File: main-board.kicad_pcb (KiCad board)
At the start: 4 copper layers, 140 x 97 mm, 30 parts, among them P1004 Rocker Switch, P10091 Molex PicoBlade 6 Right, P10092 Molex PicoBlade 6 Right, P10093 Molex PicoBlade 6 Right, P10094 Molex PicoBlade 6 Right, U10029 Small Buzzer

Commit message: Start placing parts on pcb.
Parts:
- removed ? (x4): , 
- removed B100: XT60PW, REV(5).IntLib:XT60PW
- removed Dribbler, MOTOR_2, MOTOR_3, MOTOR_4: S8B-XH-A, Miscellaneous Connectors.IntLib:S8B-XH-A-1
- removed IR: S4B-XH-A, Miscellaneous Connectors.IntLib:S4B-XH-A
- removed MOTOR_1: S8B-XH-A, ST Interface Stepper Motor Controller.IntLib:S8B-XH-A-1
- removed MikonaPOW: DS1072-2M-R, REV(5).IntLib:DS1072-2M&F-R
- removed P1004: Rocker Switch, REV(5).IntLib:Rocker_SW
- removed P10091, P10092, P10093, P10094: Molex PicoBlade 6 Right, SamatecLib.IntLib:Molex PicoBlade 6 Right SMD
- removed S_D_100: SW-PB, REV(5).IntLib:SPST-2
- removed S_ID100: ERD116RSZ, REV(5).IntLib:ERD116RSZ
- removed S_SET100: SW-DIP4, REV(5).IntLib:DIP-8-SW
- removed U10029: Small Buzzer, REV(5).IntLib:my_BUZZER
- added BZ501: Buzzer, Buzzer_Beeper:MagneticBuzzer_CUI_CMT-8504-100-SMT, F.Cu at (190.1, 140.5)
- added C201: 100nF, Capacitor_SMD:C_0603_1608Metric, F.Cu at (444.1, 21.7)
- added C301: 10nF, Capacitor_SMD:C_0805_2012Metric, F.Cu at (432.8, 80.1)
- added C302: 470nF, Capacitor_SMD:C_0603_1608Metric, F.Cu at (441.4, 79.9)
- added C303: 100nF, Capacitor_SMD:C_0603_1608Metric, F.Cu at (441.4, 82.4)
- added C304: 180nF, Capacitor_SMD:C_0603_1608Metric, F.Cu at (441.4, 84.9)
- added C305: 10uF, Capacitor_SMD:C_0805_2012Metric, F.Cu at (432.8, 83.1)
- added C306: 10uF, Capacitor_SMD:C_0805_2012Metric, F.Cu at (432.8, 86.1)
- added C307: 10uF, Capacitor_SMD:C_0805_2012Metric, F.Cu at (432.8, 89.1)
- added C308: 10uF, Capacitor_SMD:C_0805_2012Metric, F.Cu at (432.8, 92.2)
- added C309: 100nF, Capacitor_SMD:C_0603_1608Metric, F.Cu at (441.4, 87.4)
- added C310: 100uF, Capacitor_Tantalum_SMD:CP_EIA-7343-31_Kemet-D, F.Cu at (456.4, 92.9)
- added C311: 10uF 35v, Capacitor_SMD:C_0805_2012Metric, F.Cu at (432.8, 95.2)
- added C312: 10uF 35v, Capacitor_SMD:C_0805_2012Metric, F.Cu at (437.2, 80.1)
- added C313: 10uF 35v, Capacitor_SMD:C_0805_2012Metric, F.Cu at (437.2, 83.1)
- added C314: 10uF 35v, Capacitor_SMD:C_0805_2012Metric, F.Cu at (437.2, 86.1)
- added C315: 10uF 35v, Capacitor_SMD:C_0805_2012Metric, F.Cu at (437.2, 89.1)
- added C316: 10uF 35v, Capacitor_SMD:C_0805_2012Metric, F.Cu at (437.2, 92.2)
- added C317: 100nF, Capacitor_SMD:C_0603_1608Metric, F.Cu at (441.4, 89.9)
- added C318: 1.2nF, Capacitor_SMD:C_0603_1608Metric, F.Cu at (441.4, 92.4)
- added C401: 4.7nF, Capacitor_SMD:C_0603_1608Metric, F.Cu at (437.0, 141.4)
- added C402: 4.7nF, Capacitor_SMD:C_0603_1608Metric, F.Cu at (437.0, 143.9)
- added C403: 4.7nF, Capacitor_SMD:C_0603_1608Metric, F.Cu at (437.0, 146.4)
- added C404: 100nF, Capacitor_SMD:C_0603_1608Metric, F.Cu at (437.0, 148.9)
- added C405: 100nF, Capacitor_SMD:C_0603_1608Metric, F.Cu at (437.0, 151.4)
- added C406: 100nF, Capacitor_SMD:C_0603_1608Metric, F.Cu at (437.0, 154.0)
- added C407: 6pF, Capacitor_SMD:C_0603_1608Metric, F.Cu at (441.0, 141.4)
- added C408: 6pF, Capacitor_SMD:C_0603_1608Metric, F.Cu at (441.0, 143.9)
- added C501: 100nF, Capacitor_SMD:C_0603_1608Metric, F.Cu at (403.0, 117.4)
- added C502: 100nF, Capacitor_SMD:C_0603_1608Metric, F.Cu at (403.0, 119.9)
- added C503: 100nF, Capacitor_SMD:C_0603_1608Metric, F.Cu at (403.0, 122.4)
- added C504: 100nF, Capacitor_SMD:C_0603_1608Metric, F.Cu at (403.0, 124.9)
- added C505: 100nF, Capacitor_SMD:C_0603_1608Metric, F.Cu at (403.0, 127.4)
- added C506: 100nF, Capacitor_SMD:C_0603_1608Metric, F.Cu at (403.0, 129.9)
- added C507: 100nF, Capacitor_SMD:C_0603_1608Metric, F.Cu at (403.0, 132.4)
- added C508: 100nF, Capacitor_SMD:C_0603_1608Metric, F.Cu at (407.0, 117.4)
- added C509: 100nF, Capacitor_SMD:C_0603_1608Metric, F.Cu at (407.0, 119.9)
- added C510: 1uF, Capacitor_SMD:C_0603_1608Metric, F.Cu at (407.0, 122.4)
- added C511: 1uF, Capacitor_SMD:C_0603_1608Metric, F.Cu at (407.0, 124.9)
- added C512: 27pF, Capacitor_SMD:C_0603_1608Metric, F.Cu at (407.0, 127.4)
- added C513: 27pF, Capacitor_SMD:C_0603_1608Metric, F.Cu at (407.0, 129.9)
- added C514: 100nF, Capacitor_SMD:C_0603_1608Metric, F.Cu at (407.0, 132.4)
- added C601: 100nF, Capacitor_SMD:C_0603_1608Metric, F.Cu at (437.0, 117.4)
- added C602: 100nF, Capacitor_SMD:C_0603_1608Metric, F.Cu at (437.0, 119.9)
- added C603: 2.2uF, Capacitor_SMD:C_0805_2012Metric, F.Cu at (455.0, 135.2)
- added C604: 10nF, Capacitor_SMD:C_0603_1608Metric, F.Cu at (437.0, 122.4)
- added D201: LED Red, LED_SMD:LED_0603_1608Metric, F.Cu at (166.5, 91.2)
- added D202: LED Green, LED_SMD:LED_0603_1608Metric, F.Cu at (168.3, 91.2)
- added D501: LED Green, LED_SMD:LED_0603_1608Metric, F.Cu at (431.0, 147.8)
- added H101: MountingHole_Pad, MountingHole:MountingHole_3.2mm_M3_ISO14580_Pad, F.Cu at (87.5, 91.8)
- added H102: MountingHole_Pad, MountingHole:MountingHole_3.2mm_M3_ISO14580_Pad, F.Cu at (209.5, 91.8)
- added H103: MountingHole_Pad, MountingHole:MountingHole_3.2mm_M3_ISO14580_Pad, F.Cu at (109.7, 150.5)
- added H104: MountingHole_Pad, MountingHole:MountingHole_3.2mm_M3_ISO14580_Pad, F.Cu at (187.4, 150.5)
- added J101: Battery, Connector_AMASS:AMASS_XT60PW-M_1x02_P7.20mm_Horizontal, B.Cu at (122.5, 136.6)
- added J102: Mikona, 1054291104:MOLEX_1054291104, F.Cu at (413.9, 106.6)
- added J201: DSI, FH12-22S:Hirose_FH12-22S-0.5SH_1x22-1MP_P0.50mm_Horizontal, F.Cu at (175.5, 148.5)
- added J601: Qwiic, Connector_JST:JST_SH_SM04B-SRSS-TB_1x04-1MP_P1.00mm_Horizontal, F.Cu at (145.3, 59.5)
- added J602: S4B-XH-A, Connector_JST:JST_XH_S4B-XH-A_1x04_P2.50mm_Horizontal, B.Cu at (153.5, 65.9)
- added J705: ENC1, Connector_Molex:Molex_PicoBlade_53261-0671_1x06-1MP_P1.25mm_Horizontal, F.Cu at (82.6, 83.4)
- added J706: ENC2, Connector_Molex:Molex_PicoBlade_53261-0671_1x06-1MP_P1.25mm_Horizontal, F.Cu at (214.1, 83.4)
- added J707: M1, Connector_JST:JST_XH_S8B-XH-A_1x08_P2.50mm_Horizontal, B.Cu at (90.0, 77.2)
- added J708: M2, Connector_JST:JST_XH_S8B-XH-A_1x08_P2.50mm_Horizontal, B.Cu at (207.0, 59.7)
- added J711: ENC3, Connector_Molex:Molex_PicoBlade_53261-0671_1x06-1MP_P1.25mm_Horizontal, F.Cu at (214.1, 98.9)
- added J712: ENC4, Connector_Molex:Molex_PicoBlade_53261-0671_1x06-1MP_P1.25mm_Horizontal, F.Cu at (82.6, 98.9)
- added J713: M3, Connector_JST:JST_XH_S8B-XH-A_1x08_P2.50mm_Horizontal, B.Cu at (207.0, 105.3)
- added J714: M4, Connector_JST:JST_XH_S8B-XH-A_1x08_P2.50mm_Horizontal, B.Cu at (90.0, 122.8)
- added J717: ENCD, Connector_Molex:Molex_PicoBlade_53261-0671_1x06-1MP_P1.25mm_Horizontal, F.Cu at (126.9, 47.1)
- added J718: MD, Connector_JST:JST_XH_S8B-XH-A_1x08_P2.50mm_Horizontal, B.Cu at (120.0, 65.9)
- added L301: 3.3µH, Inductor_SMD:L_Bourns_SRN6045TA, F.Cu at (434.6, 100.4)
- added Module201: ComputeModule4-CM4, rpi-cm4:rpi-cm4, F.Cu at (125.7, 97.9)
- added Q301: BSC014N04LS, BSC014N04LSIATMA1:TRANS_BSC014N04LSIATMA1, F.Cu at (108.5, 141.5)
- added Q501: BSS138, Package_TO_SOT_SMD:SOT-23, F.Cu at (426.5, 148.7)
- added Q601: BSS138, Package_TO_SOT_SMD:SOT-23, F.Cu at (450.3, 135.9)
- added R101: 2mΩ, Resistor_SMD:R_2512_6332Metric, F.Cu at (424.2, 101.5)
- added R201: 0, Resistor_SMD:R_0603_1608Metric, F.Cu at (444.1, 24.3)
- added R202: 2.2K, Resistor_SMD:R_0603_1608Metric, F.Cu at (444.1, 26.8)
- added R203: 2.2K, Resistor_SMD:R_0603_1608Metric, F.Cu at (444.1, 29.3)
- added R204: 200, Resistor_SMD:R_0603_1608Metric, F.Cu at (444.1, 31.8)
- added R205: 1K, Resistor_SMD:R_0603_1608Metric, F.Cu at (444.1, 34.3)
- added R206: 1K, Resistor_SMD:R_0603_1608Metric, F.Cu at (444.1, 36.8)
- added R207: 200, Resistor_SMD:R_0603_1608Metric, F.Cu at (444.1, 39.3)
- added R301: 1mΩ, Resistor_SMD:R_2512_6332Metric, F.Cu at (443.8, 98.6)
- added R302: 2mΩ, Resistor_SMD:R_2512_6332Metric, F.Cu at (443.8, 103.5)
- added R303: 1K, Resistor_SMD:R_0603_1608Metric, F.Cu at (441.4, 94.9)
- added R304: 1M, Resistor_SMD:R_0603_1608Metric, F.Cu at (445.5, 79.9)
- added R305: 1K, Resistor_SMD:R_0603_1608Metric, F.Cu at (445.5, 82.4)
- added R306: 5.6K, Resistor_SMD:R_0603_1608Metric, F.Cu at (445.5, 84.9)
- added R307: 40.2K, Resistor_SMD:R_0603_1608Metric, F.Cu at (445.5, 87.4)
- added R308: 1K, Resistor_SMD:R_0603_1608Metric, F.Cu at (445.5, 89.9)
- added R309: 24K, Resistor_SMD:R_0603_1608Metric, F.Cu at (445.5, 92.4)
- added R310: 10, Resistor_SMD:R_0603_1608Metric, F.Cu at (445.5, 94.9)
- added R311: 1K, Resistor_SMD:R_0603_1608Metric, F.Cu at (449.5, 79.9)
- added R312: 12K 1%, Resistor_SMD:R_0603_1608Metric, F.Cu at (449.5, 82.4)
- added R313: 20K 1%, Resistor_SMD:R_0603_1608Metric, F.Cu at (449.5, 84.9)
- added R314: 2.2K 1%, Resistor_SMD:R_0603_1608Metric, F.Cu at (449.5, 87.4)
- added R401: 60.4, Resistor_SMD:R_0603_1608Metric, F.Cu at (441.0, 146.4)
- added R402: 0, Resistor_SMD:R_0603_1608Metric, F.Cu at (441.0, 148.9)
- added R403: 60.4, Resistor_SMD:R_0603_1608Metric, F.Cu at (441.0, 151.4)
- added R501: 0, Resistor_SMD:R_0603_1608Metric, F.Cu at (411.0, 117.4)
- added R502: 1K, Resistor_SMD:R_0603_1608Metric, F.Cu at (411.0, 119.9)
- added R503: 1K, Resistor_SMD:R_0603_1608Metric, F.Cu at (411.0, 122.4)
- added R504: 10K, Resistor_SMD:R_0603_1608Metric, F.Cu at (411.0, 124.9)
- added R601: 300, Resistor_SMD:R_0603_1608Metric, F.Cu at (437.0, 124.9)
- added R602: 36, Resistor_SMD:R_0603_1608Metric, F.Cu at (437.0, 127.4)
- added R603: 0, Resistor_SMD:R_0603_1608Metric, F.Cu at (437.0, 129.9)
- added RN501: 1.8K, Resistor_SMD:R_Array_Concave_4x0603, F.Cu at (426.1, 144.1)
- added RN502: 10K, Resistor_SMD:R_Array_Concave_4x0603, F.Cu at (430.3, 144.1)
- added SW201: SW_Push, Button_Switch_SMD:SW_SPST_B3U-1000P, F.Cu at (162.3, 90.4)
- added SW202: SW_Push, Button_Switch_SMD:SW_SPST_B3U-1000P, F.Cu at (158.1, 90.4)
- added SW301: SW_Push, Button_Switch_THT:SW_Tactile_SPST_Angled_PTS645Vx58-2LFS, B.Cu at (92.3, 135.6)
- added SW501: SW_Coded_SH-7050, Button_Switch_SMD:Nidec_Copal_SH-7010A, F.Cu at (139.5, 140.5)
- added SW502: SW_DIP_x04, Button_Switch_SMD:SW_DIP_SPSTx04_Slide_6.7x11.72mm_W6.73mm_P2.54mm_LowProfile_JPin, F.Cu at (151.1, 140.6)
- added SW503: S_D_2, Button_Switch_SMD:SW_Push_1P1T_NO_6x6mm_H9.5mm, F.Cu at (163.2, 140.6)
- added U1: ~, Immortals:motor-driver, F.Cu at (93.4, 86.6)
- added U2: ~, Immortals:motor-driver, F.Cu at (180.5, 86.6)
- added U201: 74154, 74HC154:DHVQFN24, F.Cu at (455.7, 55.4)
- added U202: 74LVC1G07SE-7, Package_TO_SOT_SMD:SOT-353_SC-70-5, F.Cu at (441.9, 61.4)
- added U3: ~, Immortals:motor-driver, F.Cu at (203.3, 97.9)
- added U301: LTC2955CTS8-1, Package_TO_SOT_SMD:TSOT-23-8, F.Cu at (104.7, 135.6)
- added U302: PAC1954, Package_DFN_QFN:VQFN-16-1EP_3x3mm_P0.5mm_EP1.1x1.1mm, F.Cu at (459.2, 105.5)
- added U303: LTC4231-2, Package_SO:MSOP-12_3x4mm_P0.65mm, F.Cu at (111.9, 135.0)
- added U304: AP64501SP-13, Package_SO:SOIC-8-1EP_3.9x4.9mm_P1.27mm_EP2.95x4.9mm_Mask2.71x3.4mm_ThermalVias, F.Cu at (452.4, 106.1)
- added U4: ~, Immortals:motor-driver, F.Cu at (116.2, 97.9)
- added U401: MCP251863, Package_SO:SSOP-28_5.3x10.2mm_P0.65mm, F.Cu at (448.3, 146.2)
- added U5: ~, Immortals:motor-driver, F.Cu at (148.5, 92.0)
- added U501: RP2040, Package_DFN_QFN:QFN-56-1EP_7x7mm_P0.4mm_EP3.2x3.2mm, F.Cu at (417.7, 132.2)
- added U502: 74LS151, Package_SO:SOIC-16_3.9x9.9mm_P1.27mm, F.Cu at (417.2, 121.8)
- added U503: W25Q128JVS, Package_SO:SOIC-8_5.23x5.23mm_P1.27mm, F.Cu at (418.2, 147.8)
- added U601: ICM-42688-P, ICM-42688-P:PQFN50P300X250X97-14N, F.Cu at (450.6, 131.7)
- added Y401: 40MHz, Crystal:Crystal_SMD_2016-4Pin_2.0x1.6mm, F.Cu at (444.9, 154.0)
- added Y501: 12MHz, Crystal:Crystal_SMD_5032-2Pin_5.0x3.2mm, F.Cu at (427.7, 139.3)

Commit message: Place all the components on the PCB.
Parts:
- removed Booster: S6B-XH-A, Miscellaneous Connectors.IntLib:S6B-XH-A
- C301, C302, C303, C305, C306, C307, C308, C309, C310, C311, C312, C313, C314, C315, C316, C317, C318, C401, C402, C403, C404, C405, C406, C407, C408, C501, C502, C503, C504, C505, C506, C507, C508, C509, C510, C511, L301, R101, R202, R203, R303, R305, R308, R310, R311, R312, R313, R314, R401, R402, R403, RN501, RN502, U301, U302, U304, U401, U502, Y401: moved to B.Cu
- J102: footprint 1054291104:MOLEX_1054291104 -> 1054301204:MOLEX_1054301204; moved to B.Cu
- J602: value S4B-XH-A -> IR; footprint Connector_JST:JST_XH_S4B-XH-A_1x04_P2.50mm_Horizontal -> Connector_JST:JST_SH_SM04B-SRSS-TB_1x04-1MP_P1.00mm_Horizontal
- U1, U2, U3, U4, U5: footprint Immortals:motor-driver -> Immortals:MotorDriver-SMT
- moved R303 342.5 mm to (100.9, 131.8)
- moved R307 339.8 mm to (109.5, 138.8), turned to -90 degrees
- moved R309 339.6 mm to (109.5, 142.0), turned to -90 degrees
- moved R306 337.2 mm to (111.9, 134.2), turned to -90 degrees
- moved C302 336.9 mm to (108.7, 132.6), turned to -90 degrees
- moved C301 336.3 mm to (100.7, 133.6), turned to 180 degrees
- moved R304 336.0 mm to (113.9, 134.2), turned to 90 degrees
- moved C304 334.4 mm to (112.7, 146.2), turned to -90 degrees
- moved R314 333.8 mm to (116.8, 114.5), turned to -90 degrees
- moved R312 332.5 mm to (118.2, 110.9), turned to -90 degrees
- moved U304 332.0 mm to (120.5, 116.2), turned to 90 degrees
- moved R313 330.7 mm to (119.8, 110.9), turned to 90 degrees
- moved R302 328.8 mm to (117.7, 146.0)
- moved C310 327.7 mm to (128.9, 105.4), turned to 180 degrees
- moved U302 327.6 mm to (132.3, 127.8), turned to -90 degrees
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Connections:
- J101 pad 1: +BATT -> GND
- J101 pad 2: GND -> +BATT
- J102 pad 2: GND -> /CAN_N
- J102 pad 3: /CAN_N -> /CAN_P
- J102 pad 4: /CAN_P -> GND

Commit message: Finish the draft routing.
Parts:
- removed C401, C402, C403: 4.7nF, Capacitor_SMD:C_0603_1608Metric
- removed C404, C405, C406: 100nF, Capacitor_SMD:C_0603_1608Metric
- removed C407, C408: 6pF, Capacitor_SMD:C_0603_1608Metric
- removed D1, D_D_1: LED Red 1206, Miscellaneous Devices.IntLib:3.2X1.6X1.1 - RED
- removed D2, D_D_3: LED Green 1206, Miscellaneous Devices.IntLib:3.2X1.6X1.1 - GREEN
- removed D21: LED White 1206, Miscellaneous Devices.IntLib:3.2X1.6X1.1 - WHITE
- removed D24, D_D_2: LED Yellow 1206, Miscellaneous Devices.IntLib:3.2X1.6X1.1 - YELLOW
- removed D_D_4: LED Blue 1206, Miscellaneous Devices.IntLib:3.2X1.6X1.1 - BLUE
- removed R101: 2mΩ, Resistor_SMD:R_2512_6332Metric
- removed R401, R403: 60.4, Resistor_SMD:R_0603_1608Metric
- removed R402: 0, Resistor_SMD:R_0603_1608Metric
- removed RN501: 1.8K, Resistor_SMD:R_Array_Concave_4x0603
- removed U401: MCP251863, Package_SO:SSOP-28_5.3x10.2mm_P0.65mm
- removed Y401: 40MHz, Crystal:Crystal_SMD_2016-4Pin_2.0x1.6mm
- added D301: LED Green, LED_SMD:LED_0603_1608Metric, F.Cu at (138.0, 151.0)
- added R315: 1K, Resistor_SMD:R_0603_1608Metric, F.Cu at (138.0, 147.8)
- added R505: 1.8K, Resistor_SMD:R_0603_1608Metric, B.Cu at (152.6, 58.6)
- added R506: 1.8K, Resistor_SMD:R_0603_1608Metric, B.Cu at (151.0, 58.6)
- added R507: 1.8K, Resistor_SMD:R_0603_1608Metric, F.Cu at (159.6, 80.0)
- added R508: 1.8K, Resistor_SMD:R_0603_1608Metric, B.Cu at (159.6, 80.0)
- R311: value 1K -> 2mΩ
- U202: moved to B.Cu
- moved R204 31.1 mm to (131.2, 86.5)
- moved SW201 31.1 mm to (131.2, 90.7)
- moved R207 30.2 mm to (127.9, 86.5)
- moved SW202 30.2 mm to (127.9, 90.7)
- moved R205 28.9 mm to (136.2, 93.5)
- moved D201 28.9 mm to (136.2, 90.4)
- moved U202 27.1 mm to (137.5, 95.1)
- moved RN502 26.9 mm to (159.0, 115.0), turned to 90 degrees
- moved R311 21.2 mm to (121.2, 129.6), turned to -90 degrees
- moved R305 15.1 mm to (140.1, 117.6), turned to 180 degrees
- moved U502 13.0 mm to (153.2, 123.4)
- moved C303 10.8 mm to (141.8, 120.1), turned to -90 degrees
- moved U302 9.52 mm to (138.4, 120.5), turned to 180 degrees
- moved C512 6.71 mm to (162.8, 87.4)
- moved R502 6.60 mm to (168.4, 86.4)
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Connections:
- C305 pad 1: /Power/SENSE_5v+ -> +5V
- C306 pad 1: /Power/SENSE_5v+ -> +5V
- C307 pad 1: /Power/SENSE_5v+ -> +5V
- C308 pad 1: /Power/SENSE_5v+ -> +5V
- C310 pad 1: /Power/SENSE_5v+ -> +5V
- C311 pad 1: +BATT -> /Power/SENSE_5v-
- C312 pad 1: +BATT -> /Power/SENSE_5v-
- C313 pad 1: +BATT -> /Power/SENSE_5v-
- C314 pad 1: +BATT -> /Power/SENSE_5v-
- C315 pad 1: +BATT -> /Power/SENSE_5v-
- C316 pad 1: +BATT -> /Power/SENSE_5v-
- C503 pad 1: +3V3 -> +3.3V
- C504 pad 1: +3V3 -> +3.3V
- C505 pad 1: +3V3 -> +3.3V
- C506 pad 1: +3V3 -> +3.3V
- C507 pad 1: +3V3 -> +3.3V
- C508 pad 1: +3V3 -> +3.3V
- C509 pad 1: +3V3 -> +3.3V
- C511 pad 1: +3V3 -> +3.3V
- C514 pad 1: +3V3 -> +3.3V
- J102 pad 1: /SENSE_MIKONA -> +24V
- J102 pad 2: /CAN_N -> /MICRO_I2C0_SCL
- J102 pad 3: /CAN_P -> /MICRO_I2C0_SDA
- J102 pad SH: unconnected-(J102-Shield-PadSH) -> (no net)
- L301 pad 2: /Power/SENSE_5v+ -> +5V
- Module201 pad 29: /~{CM_SPI1_CS_MICRO} -> /Compute Module/SPI1_CE2
- Module201 pad 49: /~{CM_SPI1_CS_CAN} -> /~{CM_SPI1_CS_IMU}
- Module201 pad 50: /~{CM_SPI1_CS_IMU} -> /~{CM_SPI1_CS_MICRO}
- Module201 pad 56: /~{CAN_INT} -> /Compute Module/GPIO3
- R311 pad 1: +5V -> /Power/SENSE_5v-
- R311 pad 2: /Power/SENSE_5v+ -> +BATT
- R312 pad 1: /Power/SENSE_5v+ -> +5V
- R504 pad 1: +3V3 -> +3.3V
- RN502 pad 1: /Micro/DIP_0 -> /Micro/DIP_3
- RN502 pad 2: /Micro/DIP_1 -> /Micro/DIP_2
- RN502 pad 3: /Micro/DIP_2 -> /Micro/DIP_1
- RN502 pad 4: /Micro/DIP_3 -> /Micro/DIP_0
- U201 pad 1: /~{M1_SPI_CS_C} -> /~{MD_SPI_CS_C}
- U201 pad 10: /~{MD_SPI_CS_D} -> /~{M2_SPI_CS_D}
- U201 pad 2: /~{M1_SPI_CS_D} -> /~{MD_SPI_CS_D}
- U201 pad 3: /~{M2_SPI_CS_C} -> /~{M1_SPI_CS_C}
- U201 pad 4: /~{M2_SPI_CS_D} -> /~{M1_SPI_CS_D}
- U201 pad 5: /~{M3_SPI_CS_C} -> /~{M4_SPI_CS_C}
- U201 pad 6: /~{M3_SPI_CS_D} -> /~{M4_SPI_CS_D}
- U201 pad 7: /~{M4_SPI_CS_C} -> /~{M3_SPI_CS_C}
- U201 pad 8: /~{M4_SPI_CS_D} -> /~{M3_SPI_CS_D}
- U201 pad 9: /~{MD_SPI_CS_C} -> /~{M2_SPI_CS_C}
- U302 pad 13: /Power/SENSE_5v+ -> +24V
- U302 pad 14: +5V -> /Power/SENSE_5v-
- U302 pad 7: /SENSE_MIKONA -> unconnected-(U302-SENSE3--Pad7)
- U302 pad 8: +24V -> unconnected-(U302-SENSE3+-Pad8)
- U303 pad 9: /Power/PWR_STATUS -> Net-(D301-A)
- U304 pad 2: +BATT -> /Power/SENSE_5v-
- U501 pad 1: +3V3 -> +3.3V
- U501 pad 10: +3V3 -> +3.3V
- U501 pad 15: /Micro/MUX_S0 -> /Micro/MUX_O
- U501 pad 16: /Micro/MUX_S1 -> /Micro/MUX_S2
- U501 pad 17: /Micro/MUX_S2 -> /Micro/MUX_S1
- U501 pad 18: /Micro/MUX_O -> /Micro/MUX_S0
- U501 pad 22: +3V3 -> +3.3V
- U501 pad 26: +3V3 -> +3.3V
- U501 pad 33: +3V3 -> +3.3V
- U501 pad 42: +3V3 -> +3.3V
- U501 pad 43: +3V3 -> +3.3V
- U501 pad 44: +3V3 -> +3.3V
- U501 pad 48: +3V3 -> +3.3V
- U501 pad 49: +3V3 -> +3.3V
- U501 pad 8: /MD_C_S -> /MD_D_F
- U501 pad 9: /MD_D_F -> /MD_C_S
- U502 pad 1: /Micro/DIP_3 -> /Micro/ID_BIT_2
- U502 pad 12: /Micro/ID_BIT_3 -> /Micro/DIP_0
- U502 pad 13: /Micro/ID_BIT_2 -> /Micro/DIP_1
- U502 pad 14: /Micro/ID_BIT_1 -> /Micro/DIP_2
- U502 pad 15: /Micro/ID_BIT_0 -> /Micro/DIP_3
- U502 pad 2: /Micro/DIP_2 -> /Micro/ID_BIT_0
- U502 pad 3: /Micro/DIP_1 -> /Micro/ID_BIT_1
- U502 pad 4: /Micro/DIP_0 -> /Micro/ID_BIT_3
- U503 pad 8: +3V3 -> +3.3V
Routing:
- net GND: track 0.00 -> 328.2 mm, vias 0 -> 107
- net +3.3V: track 0.00 -> 273.2 mm, vias 0 -> 35
- net /M_SPI_MISO: track 0.00 -> 206.1 mm, vias 0 -> 2
- net /M_EN: track 0.00 -> 204.3 mm, vias 0 -> 11
- net /M_SPI_MOSI: track 0.00 -> 199.8 mm, vias 0 -> 2
- net /M_SPI_SCK: track 0.00 -> 160.3 mm
- net +5V: track 0.00 -> 136.4 mm, vias 0 -> 15
- net /MICRO_I2C0_SDA: track 0.00 -> 99.0 mm, vias 0 -> 1
- net /MICRO_I2C0_SCL: track 0.00 -> 89.2 mm, vias 0 -> 1
- net /M4_D_F: track 0.00 -> 86.3 mm, vias 0 -> 2
- net /Compute Module/ID_SC: track 0.00 -> 85.6 mm, vias 0 -> 5
- net /M1_C_S: track 0.00 -> 75.1 mm, vias 0 -> 2
- net /Micro/BUTTON: track 0.00 -> 73.1 mm, vias 0 -> 2
- net /~{POWER_OFF}: track 0.00 -> 72.8 mm, vias 0 -> 3
- net /~{M1_SPI_CS_C}: track 0.00 -> 68.8 mm, vias 0 -> 2
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- added copper zone on In1.Cu, net +24V
- added copper zone on In1.Cu, net +3.3V
- added copper zone on In1.Cu, net +5V
- added copper zone on In1.Cu, net GND
- added copper zone on In2.Cu, net GND

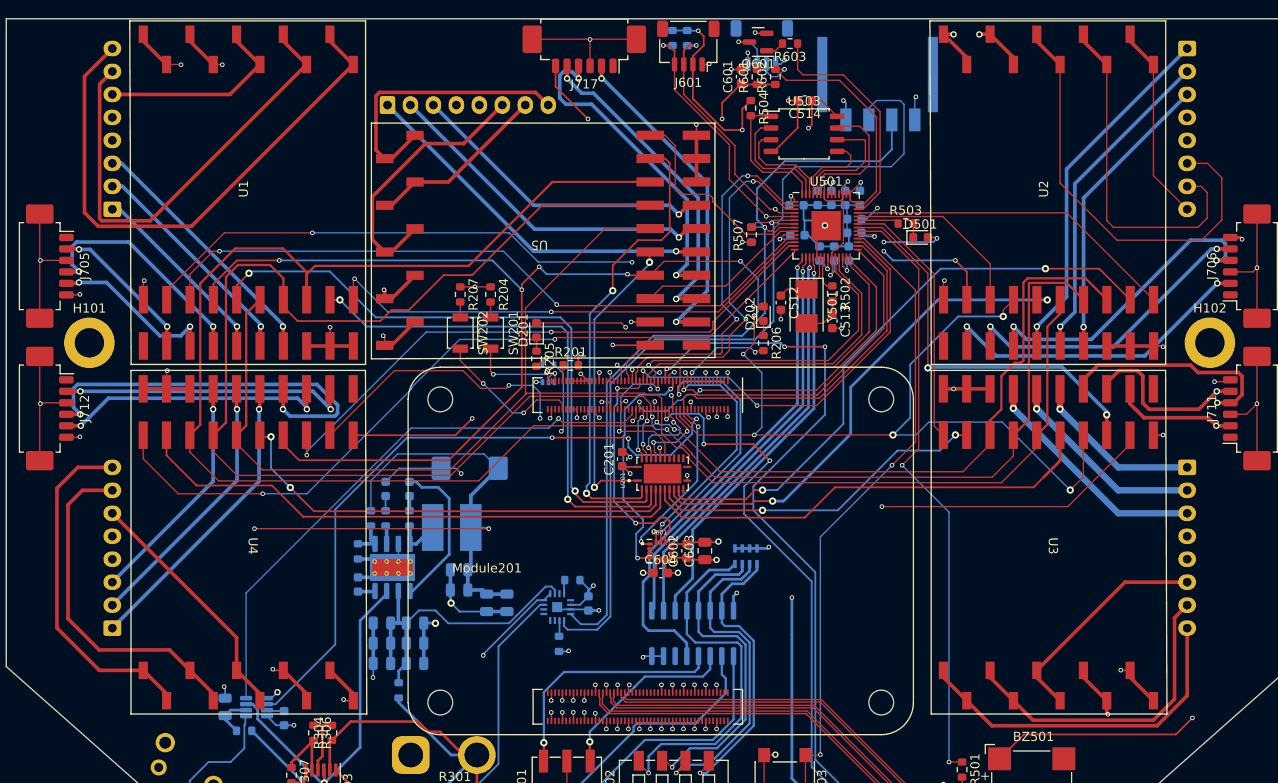
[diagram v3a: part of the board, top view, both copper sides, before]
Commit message: Fix motor winding order.
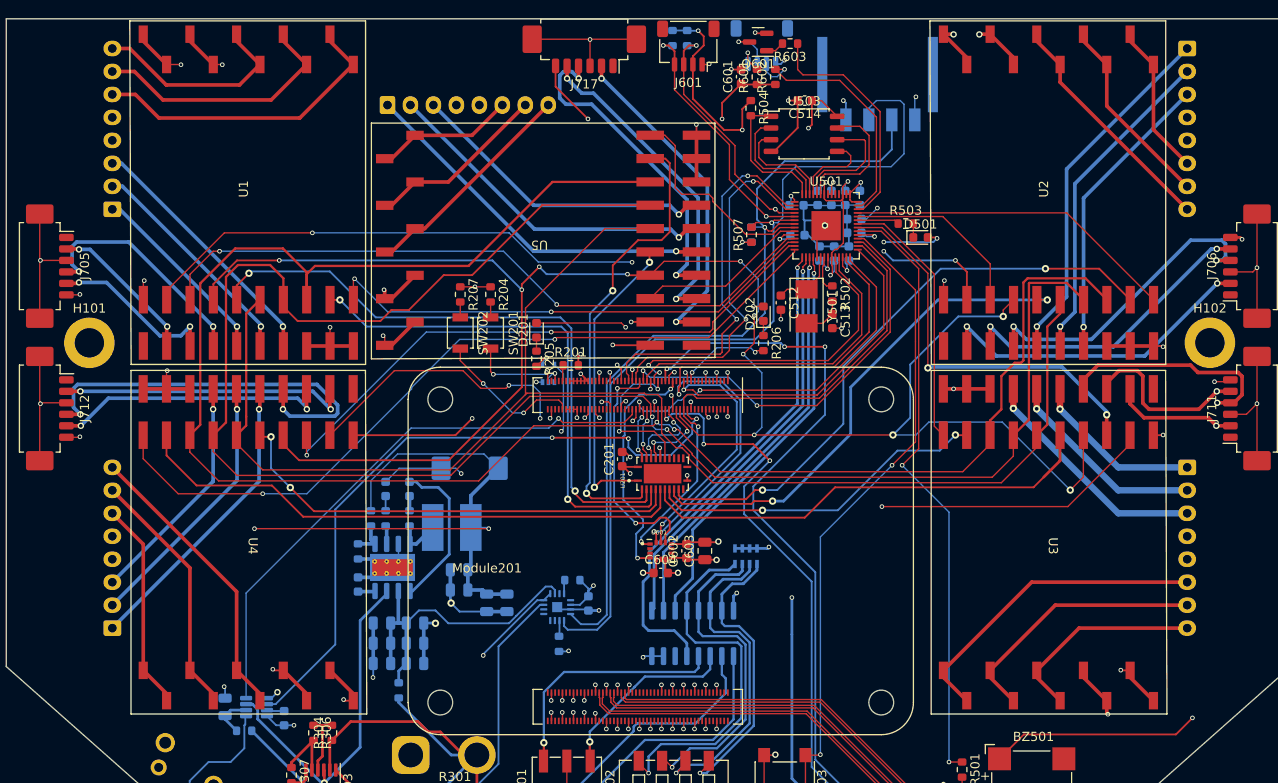
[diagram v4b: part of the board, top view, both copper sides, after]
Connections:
- J707 pad 6: /Motors/M1_U -> /Motors/M1_W
- J707 pad 8: /Motors/M1_W -> /Motors/M1_U
- J708 pad 6: /Motors/M2_U -> /Motors/M2_W
- J708 pad 8: /Motors/M2_W -> /Motors/M2_U
- J713 pad 6: /Motors/M3_U -> /Motors/M3_W
- J713 pad 8: /Motors/M3_W -> /Motors/M3_U
- J714 pad 6: /Motors/M4_U -> /Motors/M4_W
- J714 pad 8: /Motors/M4_W -> /Motors/M4_U
- J718 pad 6: /Motors/MD_U -> /Motors/MD_W
- J718 pad 8: /Motors/MD_W -> /Motors/MD_U
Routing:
- net /Motors/M1_W: track 60.6 -> 34.1 mm
- net /Motors/M1_V: track 50.6 -> 28.4 mm
- net /Motors/M2_U: track 47.4 -> 25.8 mm
- net /Motors/M2_V: track 38.2 -> 21.2 mm
- net /Motors/MD_W: track 31.1 -> 15.2 mm
- net /Motors/M4_W: track 37.8 -> 22.8 mm
- net /Motors/M4_V: track 37.8 -> 27.5 mm
- net /Motors/M3_V: track 34.5 -> 28.7 mm
- net /Motors/M4_U: track 27.1 -> 32.1 mm
- net /Motors/M2_W: track 21.6 -> 16.6 mm
- net /Motors/MD_U: track 29.2 -> 24.4 mm
- net /Motors/M3_W: track 38.2 -> 34.9 mm
- net /Motors/M3_U: track 24.7 -> 22.6 mm
- net /Motors/M1_U: track 21.8 -> 23.0 mm

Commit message: Improve routings,
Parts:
- added C515: 100nF, Capacitor_SMD:C_0603_1608Metric, B.Cu at (160.3, 119.5)
- U304: footprint Package_SO:SOIC-8-1EP_3.9x4.9mm_P1.27mm_EP2.95x4.9mm_Mask2.71x3.4mm_ThermalVias -> Package_SO:SOIC-8-1EP_3.9x4.9mm_P1.27mm_EP2.62x3.51mm
- moved R307 3.12 mm to (110.3, 135.8)
- moved R303 2.99 mm to (101.4, 134.3), turned to 90 degrees
- moved J711 2.98 mm to (214.1, 101.9)
- moved J712 2.88 mm to (82.6, 101.8)
- moved C301 1.92 mm to (100.4, 131.7), turned to 180 degrees
- moved J706 1.72 mm to (214.1, 81.7)
- moved J705 1.63 mm to (82.6, 81.8)
- moved Q501 1.61 mm to (183.1, 141.7)
- moved R501 1.61 mm to (184.1, 137.9)
- moved R309 1.43 mm to (109.6, 140.6)
- moved C302 0.78 mm to (109.5, 132.5)
- moved J602 0.48 mm to (160.7, 59.9)
- moved J601 0.43 mm to (152.7, 59.9)
- moved C304 0.13 mm to (112.6, 146.2)
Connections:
- J705 pad MP: GND -> (no net)
- J706 pad MP: GND -> (no net)
- J711 pad MP: GND -> (no net)
- J712 pad MP: GND -> (no net)
- J717 pad MP: GND -> (no net)
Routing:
- net GND: track 328.2 -> 166.7 mm, vias 107 -> 138
- net +3.3V: track 273.2 -> 202.2 mm, vias 35 -> 32
- net +5V: track 136.4 -> 96.6 mm, vias 15 -> 20
- net /Motors/M3_W: track 34.9 -> 0.00 mm
- net /Motors/M1_W: track 34.1 -> 0.00 mm
- net /Motors/M4_U: track 32.1 -> 0.00 mm
- net +24V: track 43.3 -> 11.3 mm, vias 9 -> 27
- net /Motors/M3_V: track 28.7 -> 0.00 mm
- net /Motors/M1_V: track 28.4 -> 0.00 mm
- net /Motors/M4_V: track 27.5 -> 0.00 mm
- net /Motors/M2_U: track 25.8 -> 0.00 mm
- net /Motors/MD_U: track 24.4 -> 0.00 mm
- net /Motors/M1_U: track 23.0 -> 0.00 mm
- net /Motors/M4_W: track 22.8 -> 0.00 mm
- net /Motors/M3_U: track 22.6 -> 0.00 mm
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- added copper zone on B.Cu, net +24V
- added copper zone on F.Cu, net +24V
- added copper zone on B.Cu, net +5V
- added copper zone on F.Cu, net +5V
- added copper zone on F.Cu, net +BATT
- added copper zone on F.Cu, net /Motors/M1_U
- added copper zone on F.Cu, net /Motors/M1_V
- added copper zone on F.Cu, net /Motors/M1_W
- added copper zone on F.Cu, net /Motors/M2_U
- added copper zone on F.Cu, net /Motors/M2_V
- added copper zone on F.Cu, net /Motors/M2_W
- added copper zone on F.Cu, net /Motors/M3_U
- added copper zone on F.Cu, net /Motors/M3_V
- added copper zone on F.Cu, net /Motors/M3_W
- added copper zone on F.Cu, net /Motors/M4_U
- added copper zone on F.Cu, net /Motors/M4_V
- added copper zone on F.Cu, net /Motors/M4_W
- added copper zone on F.Cu, net /Motors/MD_U
- added copper zone on F.Cu, net /Motors/MD_V
- added copper zone on F.Cu, net /Motors/MD_W
- added copper zone on F.Cu, net /Power/SENSE_24v+
- added copper zone on B.Cu, net /Power/SENSE_5v-
- added copper zone on B.Cu, net GND
- added copper zone on F.Cu, net GND
- added copper zone on F.Cu, net Net-(U303-SENSE)
- added copper zone on B.Cu, net Net-(U304-SW)

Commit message: Improve routings.
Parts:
- R311: footprint Resistor_SMD:R_0603_1608Metric -> Resistor_SMD:R_2512_6332Metric
- moved R311 9.70 mm to (130.9, 129.9)
- moved C316 4.16 mm to (119.4, 128.8), turned to 180 degrees
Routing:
- net GND: track 166.7 -> 141.5 mm, vias 138 -> 146
- net +BATT: track 70.1 -> 55.4 mm
- net /Power/SENSE_5v-: track 23.9 -> 16.2 mm
- net /Motors/M4_ENC_C: track 51.5 -> 47.2 mm
- net +3.3V: track 202.2 -> 198.2 mm
- net /~{M2_SPI_CS_D}: track 65.5 -> 69.5 mm
- net /M_SPI_MOSI: track 202.3 -> 205.5 mm
- net /M4_C_S: track 65.2 -> 62.1 mm
- net /Motors/M1_ENC_C: track 25.1 -> 28.0 mm
- net +1V1: track 20.1 -> 22.5 mm
- net /Micro/QSPI_SCLK: track 13.2 -> 10.9 mm
- net +24V: track 11.3 -> 9.15 mm, vias 27 -> 28
- net /Power/SENSE_24v+: track 47.9 -> 50.0 mm
- net /Micro/QSPI_SD3: track 14.8 -> 12.7 mm
- net /M2_D_F: track 36.1 -> 38.1 mm
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- added copper zone on B.Cu, net +3.3V
- added copper zone on B.Cu, net +BATT
